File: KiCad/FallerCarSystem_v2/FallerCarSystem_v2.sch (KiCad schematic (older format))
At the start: 2 parts

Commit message: Started ucontroller project for faller_car_ucontroller2.
Kicad projec faller_car_ucontroller2 board layout still to be done.
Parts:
- added C1, C2: 0.1uF, Capacitor_SMD:C_0603_1608Metric, symbol Device:C
- added C3, C5, C6: 4.7uF, Capacitor_SMD:C_0805_2012Metric, symbol Device:C
- added C4: 10uF, Capacitor_SMD:C_0805_2012Metric, symbol Device:C
- added D1: SMAJ5.0A/AC, Diode_SMD:D_SMA, symbol Diode:SM6T6V8A
- added D2, D3, D4: LED, LED_SMD:LED_0402_1005Metric, symbol Device:LED
- added J1, J10, J11, J12, J13, J14, J15, J16, J17, J18, J19, J2, J20, J21, J22, J23, J24, J25, J26, J27, J28, J29, J3, J30, J31, J32, J33, J34, J35, J36, J37, J38, J4, J5, J6, J7, J8, J9: Conn_01x01_Male, Connector:Finger, symbol Connector:Conn_01x01_Male
- added R1, R15, R2, R9: 4.7k, Resistor_SMD:R_0402_1005Metric, symbol Device:R
- added R10: 47k, Resistor_SMD:R_0402_1005Metric, symbol Device:R
- added R11: 22k, Resistor_SMD:R_0402_1005Metric, symbol Device:R
- added R12, R13, R14, R16, R17, R18, R19, R20, R21, R22, R23, R24, R25: 470E, Resistor_SMD:R_0402_1005Metric, symbol Device:R
- added R3: 4k7, Resistor_SMD:R_0402_1005Metric, symbol Device:R
- added R4: 5k, Resistor_SMD:R_0402_1005Metric, symbol Device:R
- added R5, R6: 200E, Resistor_SMD:R_0402_1005Metric, symbol Device:R
- added R7: 1k, Resistor_SMD:R_0402_1005Metric, symbol Device:R
- added R8: 10k, Resistor_SMD:R_0402_1005Metric, symbol Device:R
- added R?: 10E, Resistor_SMD:R_0402_1005Metric, symbol Device:R
- added U3: MCP1725-ADJE_MC_DFN-8, Package_DFN_QFN:DFN-8-1EP_3x2mm_P0.5mm_EP1.36x1.46mm, symbol FallerCarSystem_v2-rescue:MCP1725-ADJE_MC_DFN-8-Regulator_Linear
- U1: renamed from U?; footprint (none) -> Package_DFN_QFN:QFN-20-1EP_4x4mm_P0.5mm_EP2.7x2.7mm; symbol MCU_Microchip_PIC16:PIC16F15345-I_GZ -> FallerCarSystem_v2-rescue:PIC16F15345-I_GZ-MCU_Microchip_PIC16
- U2: renamed from U?; footprint Package_DFN_QFN:QFN-20-1EP_4x4mm_P0.5mm_EP2.5x2.5mm -> Package_DFN_QFN:QFN-20-1EP_4x4mm_P0.5mm_EP2.5x2.5mm_ThermalVias
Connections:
- net labels added: +3V8, +5V, EnMOT, GND, ICSPCLK, ICSPDATA, LEDA, LEDB, LEDC, LEDD, LedA, MOTOR+, PWM1, PWM2, PWM3, PWM4, PWM5, PWM6, RCS_IN, SWONOFF_OUT, UART_RX, UART_TX, VBATT, Vbatt, Vpp
- wire segments 0 -> 194
- no-connect marks 0 -> 2
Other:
- note added: "PROG1 (Fast charge current regulation)\nIreg(mA) = 1000V/Rprog1(kOhm)\n5k = 200mA"
- note added: "PROG2 (USB port current regulation select)\nPROG2 = High --> max 500mA"
- note added: "PROG3 (Charge termination)\nItermination(mA) = 1000V / Rprog3(kOhm)\n1k = 1mA"
- note added: "R1 = R2 ( (Vout-Vadj)/Vadj )\nVout = LDO Output Voltage\nVadj = ADJ Pin Voltage (typically 0.41V)\n--> Vout = 1.3V"
- note added: "THERM (Battery temperature monitor)\n10k = not used"
- moved on the sheet: U2

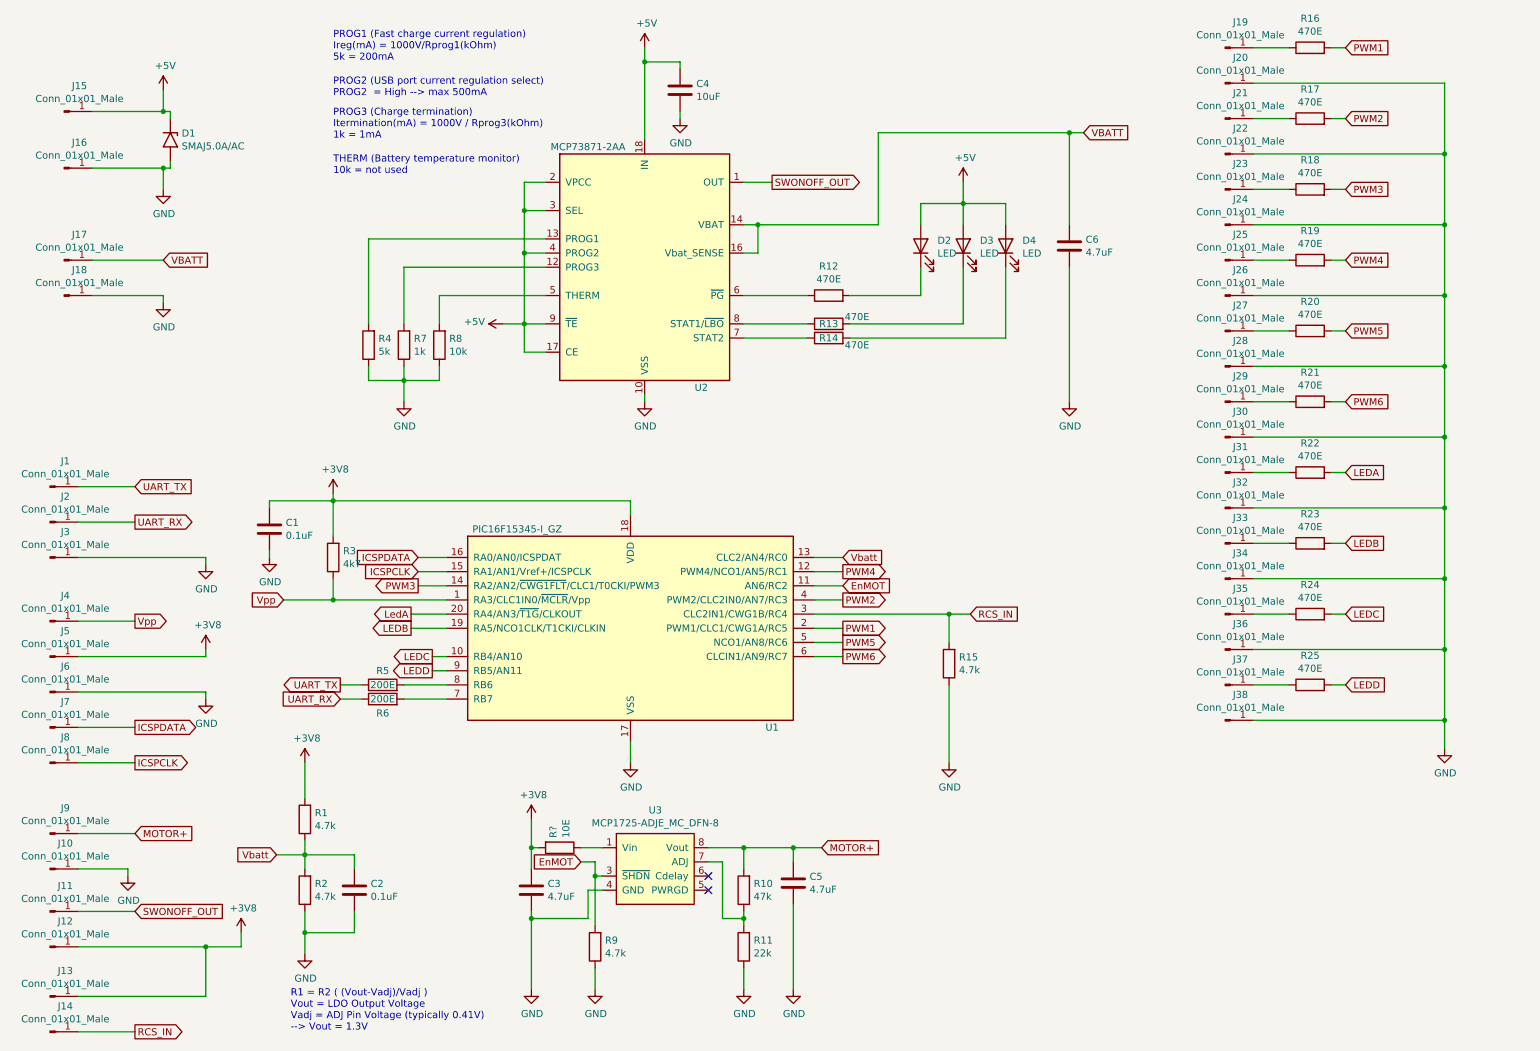
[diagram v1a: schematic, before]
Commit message: FallerCarSystem_v2 drawing and PCB done. Generated Gerber files.
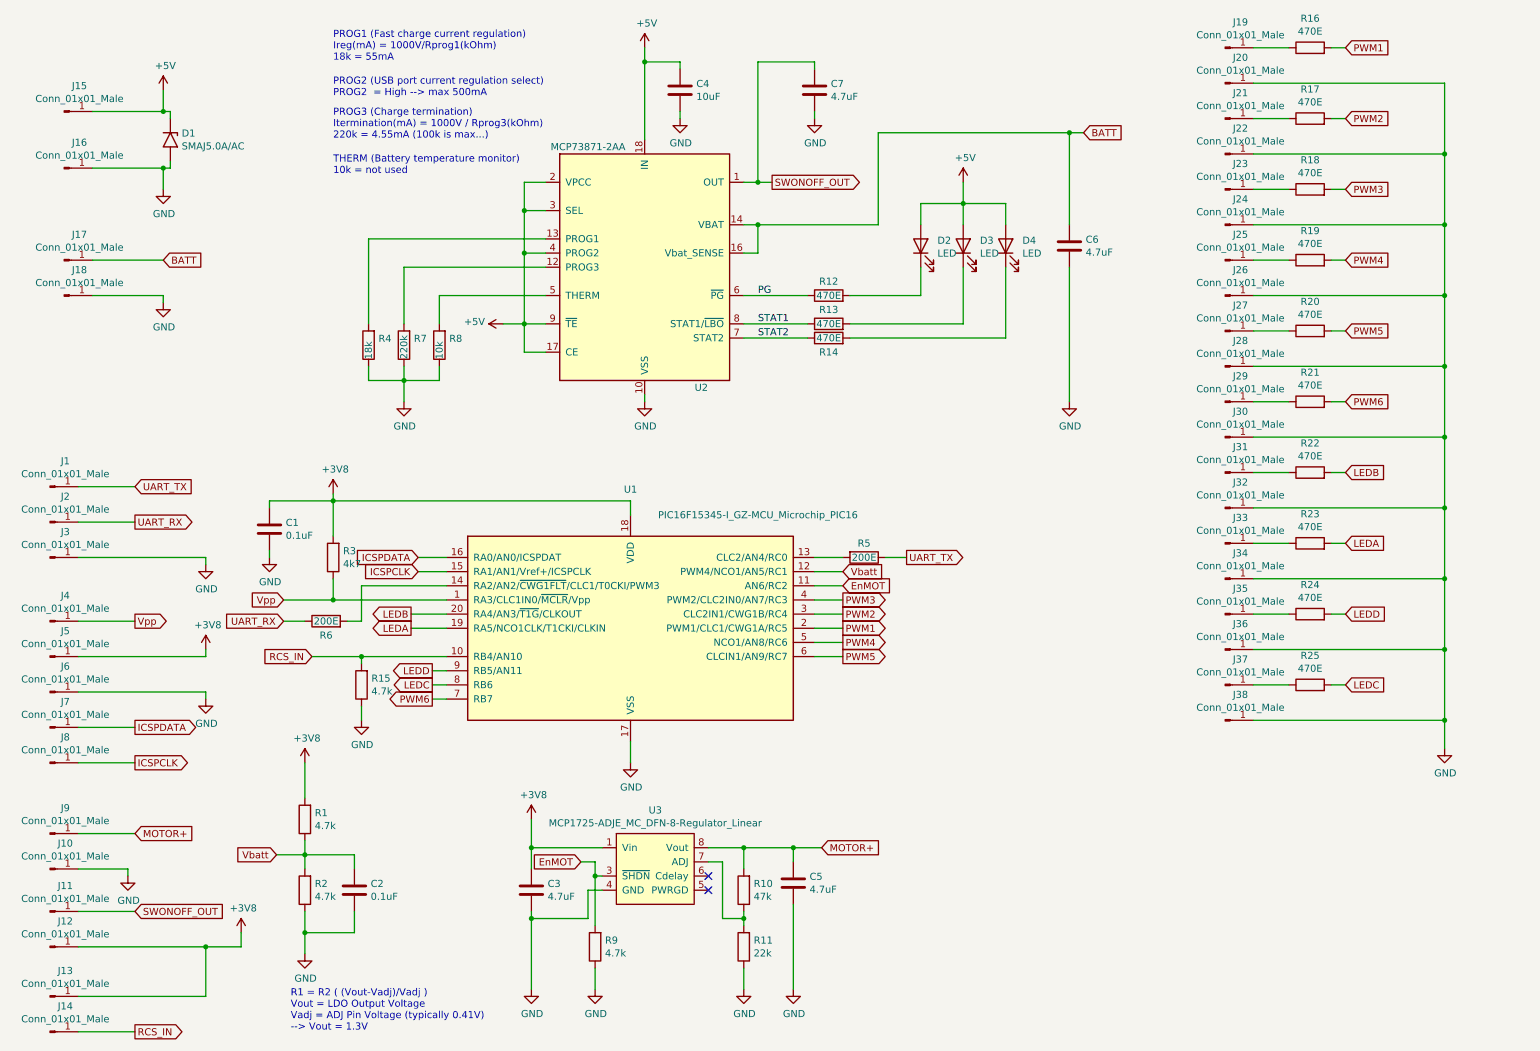
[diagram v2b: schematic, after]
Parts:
- removed R?: 10E, Resistor_SMD:R_0402_1005Metric, symbol Device:R
- added C7: 4.7uF, Capacitor_SMD:C_0805_2012Metric, symbol Device:C
- J1, J10, J11, J12, J13, J14, J15, J16, J17, J18, J19, J2, J20, J21, J22, J23, J24, J25, J26, J27, J28, J29, J3, J30, J31, J32, J33, J34, J35, J36, J37, J38, J4, J5, J6, J7, J8, J9: footprint Connector:Finger -> TestPoint:TestPoint_Pad_0.5x1.0mm
- R4: value 5k -> 18k
- R7: value 1k -> 220k
- U1: value PIC16F15345-I_GZ -> PIC16F15345-I_GZ-MCU_Microchip_PIC16; footprint Package_DFN_QFN:QFN-20-1EP_4x4mm_P0.5mm_EP2.7x2.7mm -> Package_DFN_QFN:QFN-20-1EP_4x4mm_P0.5mm_EP2.7x2.7mm_ThermalVias
- U3: value MCP1725-ADJE_MC_DFN-8 -> MCP1725-ADJE_MC_DFN-8-Regulator_Linear; footprint Package_DFN_QFN:DFN-8-1EP_3x2mm_P0.5mm_EP1.36x1.46mm -> Package_DFN_QFN:DFN-8-1EP_3x2mm_P0.5mm_EP1.36x1.46mm_ThermalVias
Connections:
- net LedA is gone; now on net LEDB: U1.20 (RA4/AN3/~T1G~/CLKOUT)
- net +3V8: now also U3.1 (Vin), U3.2 (Vin)
- net GND: now also C7.2
- net LEDA: now also R23.2, U1.19 (RA5/NCO1CLK/T1CKI/CLKIN); no longer R22.2
- net LEDB: now also R22.2; no longer R23.2, U1.19 (RA5/NCO1CLK/T1CKI/CLKIN)
- net LEDC: now also R25.2, U1.8 (RB6); no longer R24.2, U1.10 (RB4/AN10)
- net LEDD: now also R24.2; no longer R25.2
- net PWM2: now also U1.3 (CLC2IN1/CWG1B/RC4); no longer U1.4 (PWM2/CLC2IN0/AN7/RC3)
- net PWM3: now also U1.4 (PWM2/CLC2IN0/AN7/RC3); no longer U1.14 (RA2/AN2/~CWG1FLT~/CLC1/T0CKI/PWM3)
- net PWM4: now also U1.5 (NCO1/AN8/RC6); no longer U1.12 (PWM4/NCO1/AN5/RC1)
- net PWM5: now also U1.6 (CLCIN1/AN9/RC7); no longer U1.5 (NCO1/AN8/RC6)
- net PWM6: now also U1.7 (RB7); no longer U1.6 (CLCIN1/AN9/RC7)
- net RCS_IN: now also U1.10 (RB4/AN10); no longer U1.3 (CLC2IN1/CWG1B/RC4)
- net SWONOFF_OUT: now also C7.1
- net Vbatt: now also U1.12 (PWM4/NCO1/AN5/RC1); no longer U1.13 (CLC2/AN4/RC0)
- net PG: now reaches R12.1, U2.6 (~PG~)
- net STAT2: now reaches R14.1, U2.7 (STAT2)
- net STAT1: now reaches R13.1, U2.8 (STAT1/~LBO~)
- net at R6.2: now also U1.14 (RA2/AN2/~CWG1FLT~/CLC1/T0CKI/PWM3); no longer U1.7 (RB7)
- net at R5.2: now also U1.13 (CLC2/AN4/RC0); no longer U1.8 (RB6)
- net VBATT renamed BATT
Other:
- note added: "PROG1 (Fast charge current regulation)\nIreg(mA) = 1000V/Rprog1(kOhm)\n18k = 55mA"
- note added: "PROG3 (Charge termination)\nItermination(mA) = 1000V / Rprog3(kOhm)\n220k = 4.55mA (100k is max...)"
- note removed: "PROG1 (Fast charge current regulation)\nIreg(mA) = 1000V/Rprog1(kOhm)\n5k = 200mA"
- note removed: "PROG3 (Charge termination)\nItermination(mA) = 1000V / Rprog3(kOhm)\n1k = 1mA"
- moved on the sheet: R15, R5, R6

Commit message: FallerCarSystem_v2 ready and sent for production
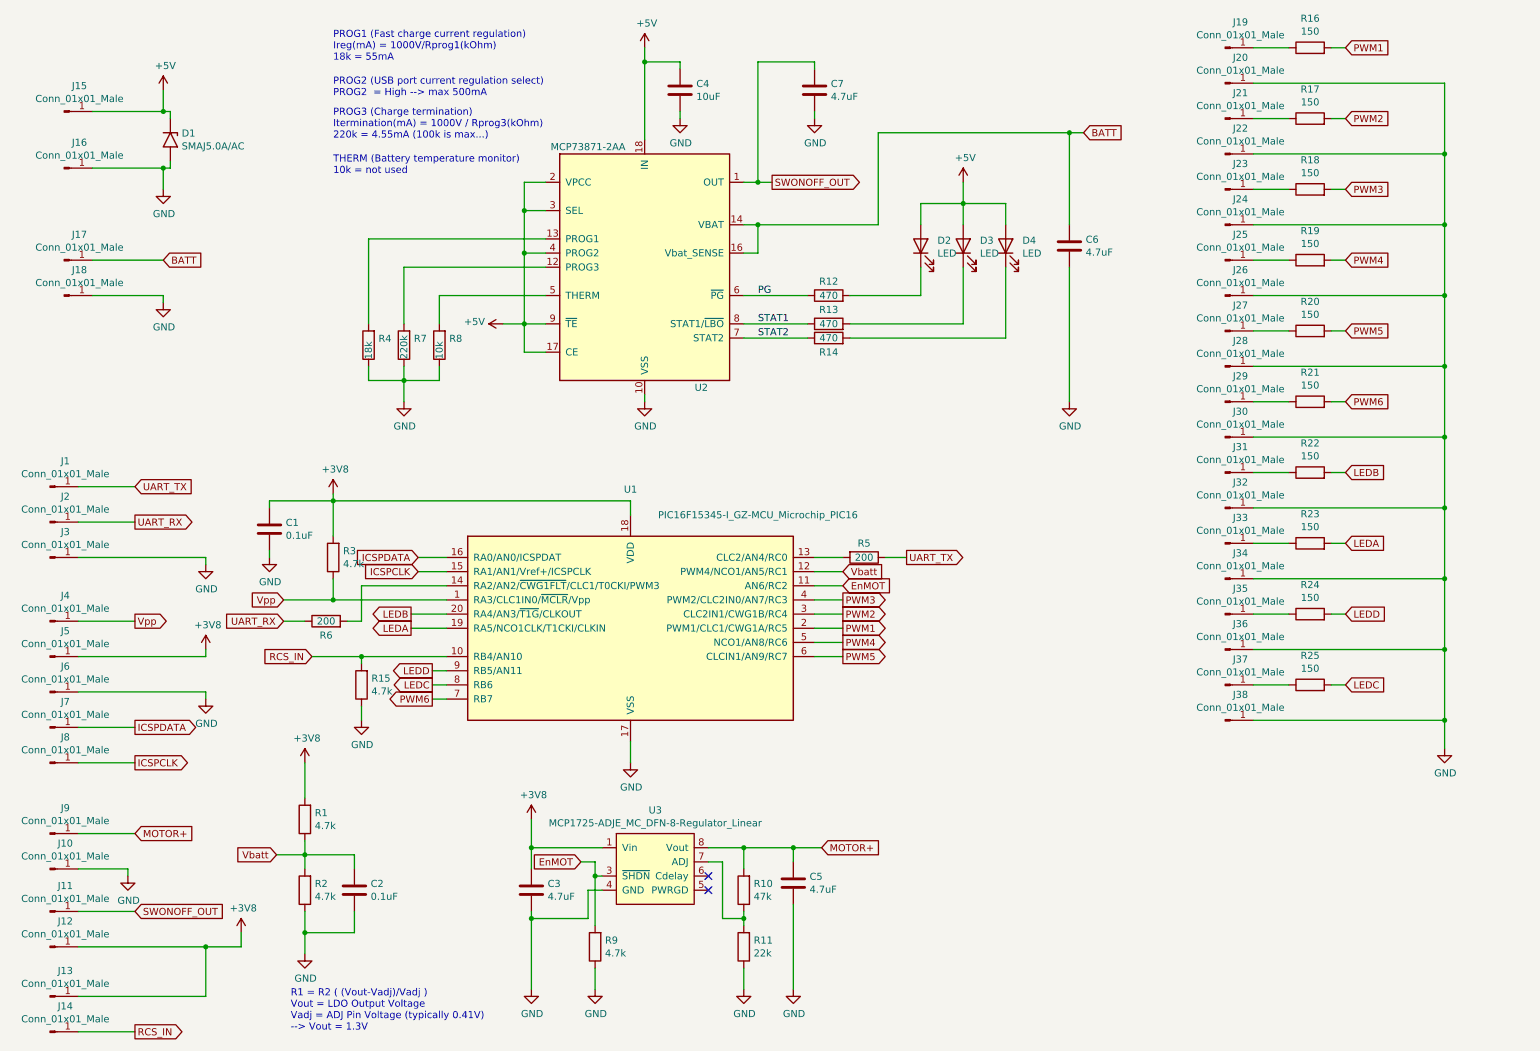
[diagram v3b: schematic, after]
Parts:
- R12, R13, R14: value 470E -> 470
- R16, R17, R18, R19, R20, R21, R22, R23, R24, R25: value 470E -> 150
- R3: value 4k7 -> 4.7k
- R5, R6: value 200E -> 200
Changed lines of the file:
@@
 P 6300 2500
 F 0 "R12" V 6400 2500 50  0000 C CNN
-F 1 "470E" V 6300 2500 50  0000 C CNN
+F 1 "470" V 6300 2500 50  0000 C CNN
 F 2 "Resistor_SMD:R_0402_1005Metric" V 6230 2500 50  0001 C CNN
 F 3 "~" H 6300 2500 50  0001 C CNN
@@
 P 6300 2700
 F 0 "R13" V 6400 2700 50  0000 C CNN
-F 1 "470E" V 6300 2700 50  0000 C CNN
+F 1 "470" V 6300 2700 50  0000 C CNN
 F 2 "Resistor_SMD:R_0402_1005Metric" V 6230 2700 50  0001 C CNN
 F 3 "~" H 6300 2700 50  0001 C CNN
@@
 P 6300 2800
 F 0 "R14" V 6200 2800 50  0000 C CNN
-F 1 "470E" V 6300 2800 50  0000 C CNN
+F 1 "470" V 6300 2800 50  0000 C CNN
 F 2 "Resistor_SMD:R_0402_1005Metric" V 6230 2800 50  0001 C CNN
 F 3 "~" H 6300 2800 50  0001 C CNN
@@
 P 2800 4350
 F 0 "R3" H 2730 4304 50  0000 R CNN
-F 1 "4k7" H 2730 4395 50  0000 R CNN
+F 1 "4.7k" H 2730 4395 50  0000 R CNN
 F 2 "Resistor_SMD:R_0402_1005Metric" V 2730 4350 50  0001 C CNN
 F 3 "~" H 2800 4350 50  0001 C CNN
@@
 P 6550 4350
 F 0 "R5" V 6450 4350 50  0000 C CNN
-F 1 "200E" V 6550 4350 50  0000 C CNN
+F 1 "200" V 6550 4350 50  0000 C CNN
 F 2 "Resistor_SMD:R_0402_1005Metric" V 6480 4350 50  0001 C CNN
 F 3 "~" H 6550 4350 50  0001 C CNN
@@
 P 2750 4800
 F 0 "R6" V 2650 4800 50  0000 C CNN
-F 1 "200E" V 2750 4800 50  0000 C CNN
+F 1 "200" V 2750 4800 50  0000 C CNN
 F 2 "Resistor_SMD:R_0402_1005Metric" V 2680 4800 50  0001 C CNN
 F 3 "~" H 2750 4800 50  0001 C CNN
@@
 P 9700 750
 F 0 "R16" V 9907 750 50  0000 C CNN
-F 1 "470E" V 9816 750 50  0000 C CNN
+F 1 "150" V 9816 750 50  0000 C CNN
 F 2 "Resistor_SMD:R_0402_1005Metric" V 9630 750 50  0001 C CNN
 F 3 "~" H 9700 750 50  0001 C CNN
@@
 P 9700 1250
 F 0 "R17" V 9907 1250 50  0000 C CNN
-F 1 "470E" V 9816 1250 50  0000 C CNN
+F 1 "150" V 9816 1250 50  0000 C CNN
 F 2 "Resistor_SMD:R_0402_1005Metric" V 9630 1250 50  0001 C CNN
 F 3 "~" H 9700 1250 50  0001 C CNN
@@
 P 9700 1750
 F 0 "R18" V 9907 1750 50  0000 C CNN
-F 1 "470E" V 9816 1750 50  0000 C CNN
+F 1 "150" V 9816 1750 50  0000 C CNN
 F 2 "Resistor_SMD:R_0402_1005Metric" V 9630 1750 50  0001 C CNN
 F 3 "~" H 9700 1750 50  0001 C CNN
@@
 P 9700 2250
 F 0 "R19" V 9907 2250 50  0000 C CNN
-F 1 "470E" V 9816 2250 50  0000 C CNN
+F 1 "150" V 9816 2250 50  0000 C CNN
 F 2 "Resistor_SMD:R_0402_1005Metric" V 9630 2250 50  0001 C CNN
 F 3 "~" H 9700 2250 50  0001 C CNN
@@
 P 9700 2750
 F 0 "R20" V 9907 2750 50  0000 C CNN
-F 1 "470E" V 9816 2750 50  0000 C CNN
+F 1 "150" V 9816 2750 50  0000 C CNN
 F 2 "Resistor_SMD:R_0402_1005Metric" V 9630 2750 50  0001 C CNN
 F 3 "~" H 9700 2750 50  0001 C CNN
@@
 P 9700 3250
 F 0 "R21" V 9907 3250 50  0000 C CNN
-F 1 "470E" V 9816 3250 50  0000 C CNN
+F 1 "150" V 9816 3250 50  0000 C CNN
 F 2 "Resistor_SMD:R_0402_1005Metric" V 9630 3250 50  0001 C CNN
 F 3 "~" H 9700 3250 50  0001 C CNN
@@
 P 9700 3750
 F 0 "R22" V 9907 3750 50  0000 C CNN
-F 1 "470E" V 9816 3750 50  0000 C CNN
+F 1 "150" V 9816 3750 50  0000 C CNN
 F 2 "Resistor_SMD:R_0402_1005Metric" V 9630 3750 50  0001 C CNN
 F 3 "~" H 9700 3750 50  0001 C CNN
@@
 P 9700 4250
 F 0 "R23" V 9907 4250 50  0000 C CNN
-F 1 "470E" V 9816 4250 50  0000 C CNN
+F 1 "150" V 9816 4250 50  0000 C CNN
 F 2 "Resistor_SMD:R_0402_1005Metric" V 9630 4250 50  0001 C CNN
 F 3 "~" H 9700 4250 50  0001 C CNN
@@
 P 9700 4750
 F 0 "R24" V 9907 4750 50  0000 C CNN
-F 1 "470E" V 9816 4750 50  0000 C CNN
+F 1 "150" V 9816 4750 50  0000 C CNN
 F 2 "Resistor_SMD:R_0402_1005Metric" V 9630 4750 50  0001 C CNN
 F 3 "~" H 9700 4750 50  0001 C CNN
@@
 P 9700 5250
 F 0 "R25" V 9907 5250 50  0000 C CNN
-F 1 "470E" V 9816 5250 50  0000 C CNN
+F 1 "150" V 9816 5250 50  0000 C CNN
 F 2 "Resistor_SMD:R_0402_1005Metric" V 9630 5250 50  0001 C CNN
 F 3 "~" H 9700 5250 50  0001 C CNN

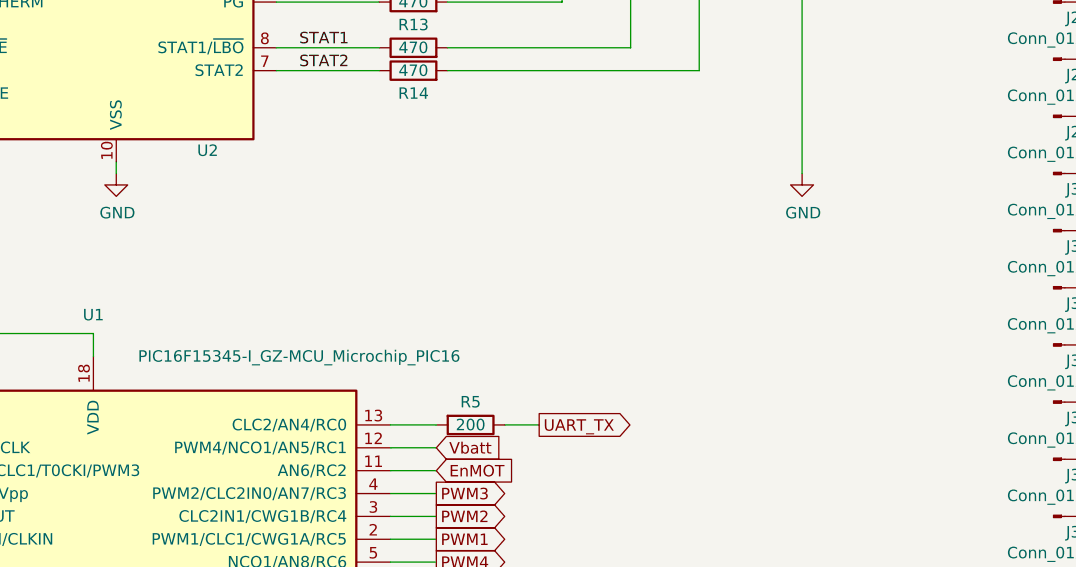
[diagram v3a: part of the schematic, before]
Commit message: Various updates. Still trying to find out why the bootloader cannot erase and write to PFM via NVMREG...
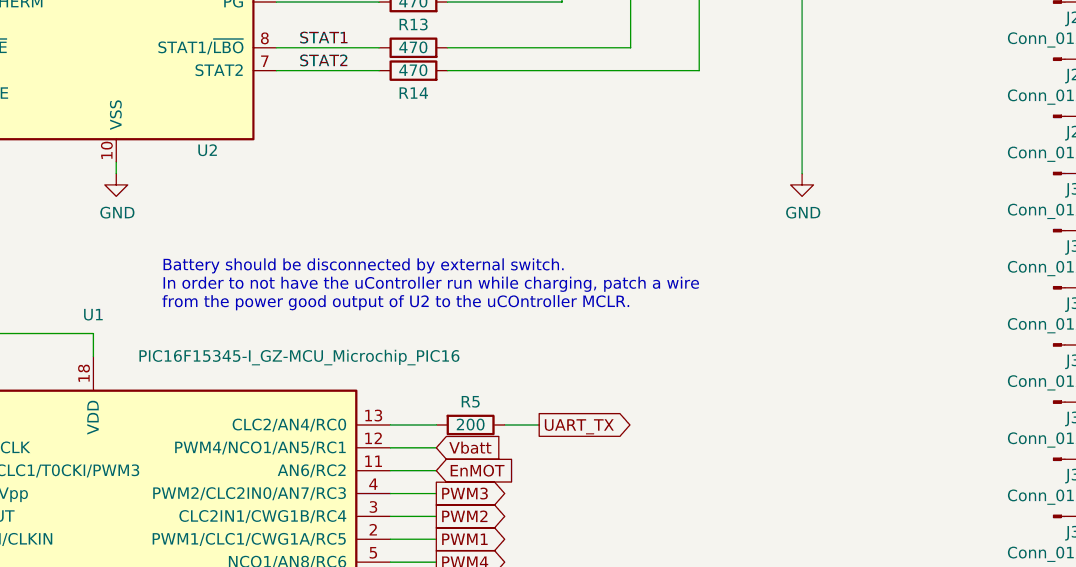
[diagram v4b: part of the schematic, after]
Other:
- note added: "Battery should be disconnected by external switch.\nIn order to not have the uController run while charging, patch a wire\nfrom the power good output of U2 to the uCOntroller MCLR."
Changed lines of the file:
@@
 Wire Wire Line
 	5800 1700 5700 1700
+Text Notes 5200 3850 0    50   ~ 0
+Battery should be disconnected by external switch.\nIn order to not have the uController run while charging, patch a wire\nfrom the power good output of U2 to the uCOntroller MCLR.
 $EndSCHEMATC
